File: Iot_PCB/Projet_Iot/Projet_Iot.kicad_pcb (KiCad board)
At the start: 2 copper layers, 33 parts, among them J10 110990030, J11 110990030, J12 110990030, J13 110990030, J14 110990030, J15 110990030, J16 110990030, J17 110990030, J18 110990030, J21 Conn_01x15_Pin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

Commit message: pcb mis à jour
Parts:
- removed J37, J39, J41, J43: 110990030, Grove:SEEED_110990030
- removed R16: R, Resistor_THT:R_Axial_DIN0207_L6.3mm_D2.5mm_P10.16mm_Horizontal
- removed U10: 74LS151, Package_DIP:DIP-16_W7.62mm
- removed U11: FDC6326L, FDC6326L:SOT95P280X110-6N
- added REF**: SOT95P280X110-6N, FDC6326L:SOT95P280X110-6N, F.Cu at (117.0, 127.8)
- U7: value 74LS151 -> mx8v1_74LS151
- moved J42 179.6 mm to (23.0, 121.5), turned to 180 degrees
- moved J36 179.4 mm to (22.5, 94.5), turned to 180 degrees
- moved J38 179.3 mm to (22.5, 76.0), turned to 180 degrees
- moved J40 178.8 mm to (23.0, 106.0), turned to 180 degrees
- moved U7 163.4 mm to (45.4, 78.4)
- moved J10 153.6 mm to (150.0, 24.5), turned to 90 degrees
- moved J15 138.9 mm to (113.3, 20.5), turned to 90 degrees
- moved J21 137.4 mm to (265.0, 129.2), turned to 180 degrees
- moved J24 122.4 mm to (126.0, 84.5)
- moved J9 116.8 mm to (85.5, 17.5), turned to 90 degrees
- moved J22 116.7 mm to (249.8, 129.1), turned to 180 degrees
- moved J8 113.1 mm to (93.0, 18.5), turned to 90 degrees
- moved J18 47.0 mm to (86.0, 168.0), turned to -90 degrees
- moved R14 32.2 mm to (162.8, 41.5)
- moved J7 27.8 mm to (129.0, 19.5), turned to 90 degrees
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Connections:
- J23 pad 4: /GND -> /3v3
- U6 pad 1: /GND -> unconnected-(U11-R2-Pad1)
- U6 pad 31: /3v3 -> (no net)
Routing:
- net /GND: track 0.00 -> 674.3 mm
- net /3v3: track 0.00 -> 537.0 mm
- net /1_Wire: track 0.00 -> 157.9 mm
- net /SDA: track 0.00 -> 104.5 mm
- net /Ventillateur_Signal: track 0.00 -> 101.8 mm
- net /Grove2-3: track 0.00 -> 101.3 mm
- net /Grove1-2: track 0.00 -> 99.5 mm
- net /SDL: track 0.00 -> 99.2 mm
- net /Grove1-1: track 0.00 -> 96.0 mm
- net /Grove3-3: track 0.00 -> 79.0 mm
- net /DHT22_IN: track 0.00 -> 78.3 mm
- net /Mux8v1_capt_hum1/Hum6: track 0.00 -> 48.0 mm
- net /Mux8v1_capt_hum1/Hum4: track 0.00 -> 45.3 mm
- net /Mux8v1_capt_hum1/Hum7: track 0.00 -> 44.1 mm
- net /Mux8v1_capt_hum1/Hum5: track 0.00 -> 41.1 mm
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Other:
- board text added: "Capteur de température"
- board text added: "Capteur humidité"
- board text added: "Capteur lumière"
- board text added: "Capteur o2/co2"
- board text added: "DHT22"
- board text added: "Grove bonus"
- board text added: "Lora"
- board text added: "Nano(IA)"
- board text added: "Ventillateur"

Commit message: pcb and schematic up to date
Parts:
- removed J10, J12, J13, J15, J16, J6, J7: 110990030, Grove:SEEED_110990030
- removed J21, J22: Conn_01x15_Pin, Connector_PinHeader_2.54mm:PinHeader_1x15_P2.54mm_Vertical
- removed R14: 4700, Resistor_THT:R_Axial_DIN0207_L6.3mm_D2.5mm_P10.16mm_Horizontal
- removed REF**: SOT95P280X110-6N, FDC6326L:SOT95P280X110-6N
- added ?: , , F.Cu at (71.3, 52.8)
- added ?: , , F.Cu at (71.3, 60.5)
- added ?: , , F.Cu at (71.3, 50.3)
- added ?: , , F.Cu at (71.3, 57.9)
- added ?: , , F.Cu at (71.3, 55.4)
- added R6: 1000, Resistor_THT:R_Axial_DIN0207_L6.3mm_D2.5mm_P10.16mm_Horizontal, F.Cu at (129.7, 124.0)
- added R7: 100, Resistor_THT:R_Axial_DIN0207_L6.3mm_D2.5mm_P10.16mm_Horizontal, F.Cu at (127.2, 131.6)
- added R7: 100, Resistor_THT:R_Axial_DIN0207_L6.3mm_D2.5mm_P10.16mm_Horizontal, F.Cu at (101.8, 134.1)
- added U11: FDC6326L, FDC6326L:SOT95P280X110-6N, B.Cu at (115.8, 126.5)
- added U7: EMC2301-x-ACZL, Package_SO:MSOP-8_3x3mm_P0.65mm, B.Cu at (114.5, 52.8)
- moved J11 90.1 mm to (111.5, 80.8)
- moved J14 82.9 mm to (112.9, 88.4)
- moved J17 39.9 mm to (58.6, 129.5)
- moved J18 39.4 mm to (86.5, 128.6)
- moved J23 38.5 mm to (68.7, 128.6)
- moved J9 35.7 mm to (78.0, 52.4)
- moved J8 34.0 mm to (86.5, 51.8)
- moved J24 28.7 mm to (98.8, 93.5)
- moved J42 24.1 mm to (35.8, 101.1)
- moved J40 17.9 mm to (35.8, 93.5)
- moved J36 15.9 mm to (35.8, 85.9)
- moved D6 13.0 mm to (132.0, 105.7)
- moved R15 13.0 mm to (109.4, 106.2)
- moved J38 13.0 mm to (35.3, 78.2)
- moved U6 10.3 mm to (77.4, 90.1)
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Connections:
- J23 pad 4: /3v3 -> /GND
- U6 pad 22: unconnected-(U6-GPIO19-Pad22) -> /interrupt_ia
- U6 pad 3: /ADC2 -> unconnected-(U6-GPIO39-Pad3)
- U6 pad 30: unconnected-(U6-GPIO15-Pad30) -> /Enable_LS
- U6 pad 31: (no net) -> /3v3_ESP
- U6 pad 9: /Ventillateur_Signal -> unconnected-(U6-GPIO26-Pad9)
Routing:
- net /3v3: track 537.0 -> 243.3 mm, vias 0 -> 2
- net /GND: track 674.3 -> 431.1 mm, vias 0 -> 2
- net /1_Wire: track 157.9 -> 38.7 mm
- net /Ventillateur_Signal: track 101.8 -> 0.00 mm
- net /DHT22_IN: track 78.3 -> 0.00 mm
- net /Enable_LS: track 0.00 -> 74.9 mm, vias 0 -> 3
- net /Grove1-1: track 96.0 -> 35.6 mm
- net /3v3_ESP: track 0.00 -> 59.4 mm
- net /Grove1-2: track 99.5 -> 44.4 mm
- net /Grove2-3: track 101.3 -> 55.3 mm
- net (no net): track 37.1 -> 0.00 mm
- net /intterupt_ia: track 0.00 -> 30.6 mm
- net /Grove3-3: track 79.0 -> 49.5 mm
- net /SDL: track 99.2 -> 70.4 mm
- net /SDA: track 104.5 -> 82.6 mm
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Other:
- board text added: "Capteur de température sol"
- board text added: "IA pin"
- board text removed: "Capteur de température"
- board text removed: "DHT22"
- board text removed: "Nano(IA)"

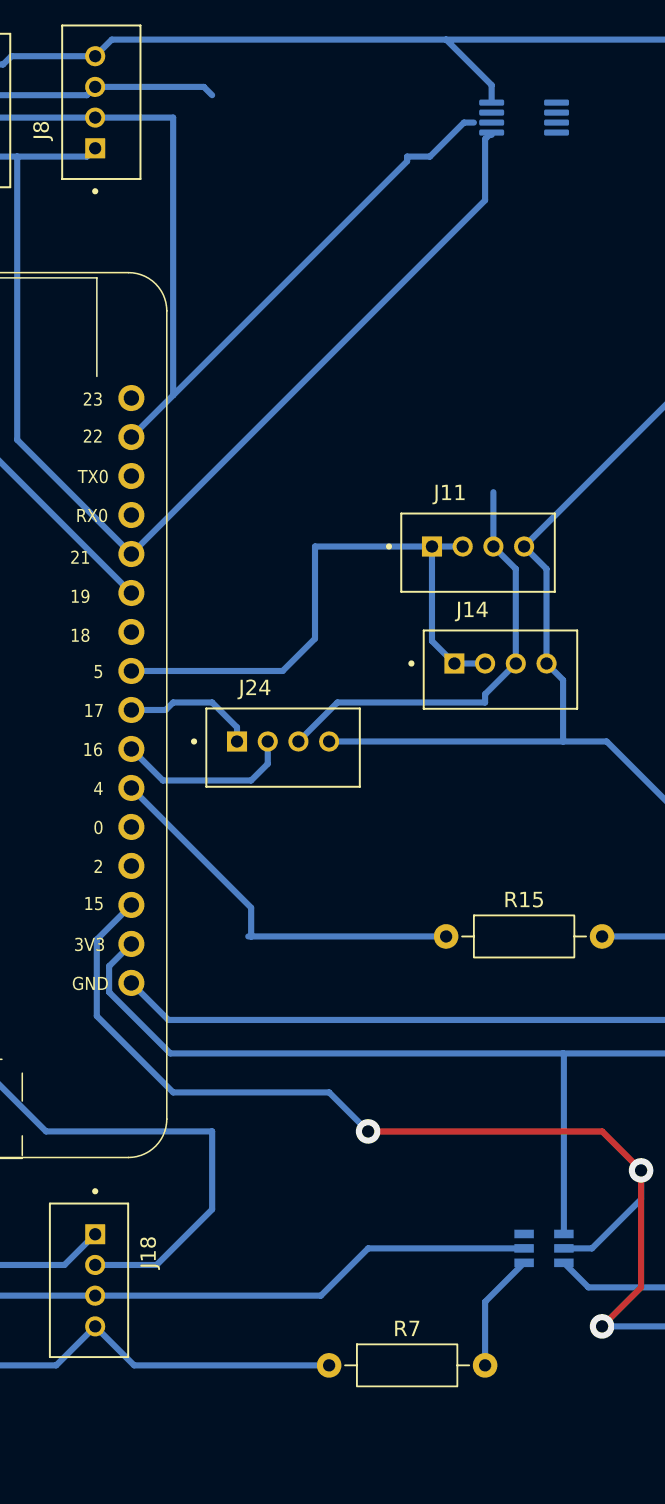
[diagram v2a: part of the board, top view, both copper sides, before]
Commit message: pcb upgraded, adding the forgotten capacitor
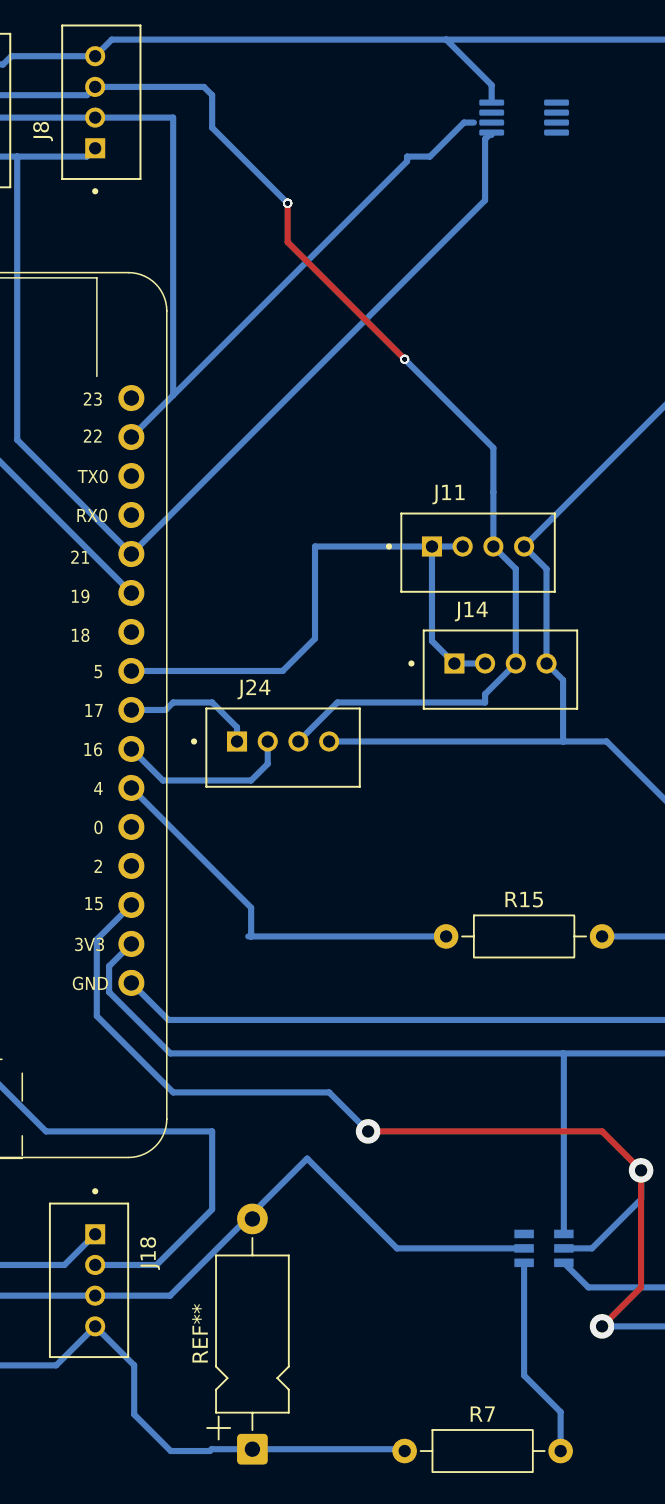
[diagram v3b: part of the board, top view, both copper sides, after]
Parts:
- added REF**: CP_Axial_L10.0mm_D4.5mm_P15.00mm_Horizontal, Capacitor_THT:CP_Axial_L10.0mm_D4.5mm_P15.00mm_Horizontal, F.Cu at (96.8, 139.6)
- R7: value 100 -> 4700
- moved R7 7.44 mm to (106.7, 139.7)
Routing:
- net /3v3: track 243.3 -> 281.6 mm, vias 2 -> 7
- net /GND: track 431.1 -> 440.3 mm
- net Net-(U11-R2): track 7.73 -> 13.2 mm

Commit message: final version of pcb
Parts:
- removed the ? at (71.3, 52.8)
- removed the ? at (71.3, 60.5)
- removed the ? at (71.3, 50.3)
- removed the ? at (71.3, 57.9)
- removed the ? at (71.3, 55.4)
- removed D6: LED, LED_THT:LED_D5.0mm
- removed R15: 10000, Resistor_THT:R_Axial_DIN0207_L6.3mm_D2.5mm_P10.16mm_Horizontal
- removed the R7 at (127.2, 131.6)
- removed the R7 at (106.7, 139.7)
- removed the REF** at (96.8, 139.6)
- removed the U7 at (114.5, 52.8)
- added ?: , , F.Cu at (101.6, 68.5)
- added ?: , , F.Cu at (86.3, 68.5)
- added J8: 110990030, Grove:SEEED_110990030, F.Cu at (81.1, 30.9)
- added J8: 110990030, Grove:SEEED_110990030, F.Cu at (88.7, 29.5)
- added R10: 4700, Resistor_THT:R_Axial_DIN0207_L6.3mm_D2.5mm_P10.16mm_Horizontal, F.Cu at (100.3, 88.9)
- added R7: 100, Resistor_THT:R_Axial_DIN0207_L6.3mm_D2.5mm_P10.16mm_Horizontal, F.Cu at (86.4, 96.5)
- added REF**: MountingHole_2.1mm, MountingHole:MountingHole_2.1mm, F.Cu at (20.3, 24.1)
- added REF**: MountingHole_2.1mm, MountingHole:MountingHole_2.1mm, F.Cu at (105.4, 24.1)
- added REF**: MountingHole_2.1mm, MountingHole:MountingHole_2.1mm, F.Cu at (20.3, 96.5)
- added REF**: MountingHole_2.1mm, MountingHole:MountingHole_2.1mm, F.Cu at (105.4, 96.5)
- added REF**: CP_Elec_5x3, Capacitor_SMD:CP_Elec_5x3, B.Cu at (81.1, 94.0)
- moved U11 49.1 mm to (91.4, 83.8)
- moved J17 47.8 mm to (43.2, 84.3)
- moved R6 47.6 mm to (104.1, 83.8)
- moved J14 36.4 mm to (97.5, 55.4)
- moved J18 36.4 mm to (71.1, 95.6)
- moved J23 36.4 mm to (53.3, 95.6)
- moved J24 36.4 mm to (83.4, 60.5)
- moved J36 36.4 mm to (20.4, 52.9)
- moved J40 36.4 mm to (20.4, 60.5)
- moved J42 36.4 mm to (20.4, 68.1)
- moved U6 36.4 mm to (62.0, 57.1)
- moved U7 36.4 mm to (33.0, 47.8)
- moved J11 36.4 mm to (96.1, 47.8)
- moved J38 36.4 mm to (19.9, 45.3)
- moved J9 31.5 mm to (62.6, 24.9)
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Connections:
- J24 pad 1: Net-(U6-GPIO17) -> Net-(U6-GPIO16)
- J24 pad 2: Net-(U6-GPIO16) -> Net-(U6-GPIO17)
- U6 pad 2: /ADC1 -> unconnected-(U6-GPIO39-Pad3)
- U6 pad 3: unconnected-(U6-GPIO39-Pad3) -> /ADC2
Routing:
- net /GND: track 440.3 -> 32.6 mm
- net /3v3_ESP: track 59.4 -> 107.6 mm
- net /SDL: track 70.4 -> 34.8 mm
- net /intterupt_ia: track 30.6 -> 0.00 mm
- net /interrupt_ia: track 0.00 -> 28.1 mm
- net /SDA: track 82.6 -> 54.9 mm
- net /Enable_LS: track 74.9 -> 52.5 mm, vias 3 -> 2
- net /Grove1-1: track 35.6 -> 24.4 mm
- net /Grove3-3: track 49.5 -> 38.5 mm
- net Net-(D6-A): track 10.2 -> 0.00 mm
- net Net-(U11-R1,C1): track 15.4 -> 25.2 mm
- net Net-(U6-GPIO4): track 25.8 -> 16.1 mm
- net /3v3: track 281.6 -> 290.1 mm, vias 7 -> 2
- net Net-(U6-GPIO16): track 11.6 -> 7.08 mm
- net /Grove1-2: track 44.4 -> 40.2 mm
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- added copper zone on B.Cu, net /GND
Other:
- board outline added: 100.3 x 87.6 mm
- board text added: "BUZZER IHM"
- board text added: "Capteur de température"
- board text added: "Fallou Quentin Yanis Vinh Taha"
- board text removed: "Capteur de température sol"

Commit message: correction pcb final
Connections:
- U7 pad 4: /Mux8v1_capt_hum1/Hum0 -> /ADC2
- U7 pad 5: /ADC2 -> /Mux8v1_capt_hum1/Hum0
- U7 pad 6: unconnected-(U7-~{Z}-Pad6) -> /GND
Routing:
- net /GND: track 32.6 -> 35.1 mm
- net /ADC2: track 26.4 -> 24.3 mm
- net /Mux8v1_capt_hum1/Hum0: track 11.0 -> 11.7 mm
